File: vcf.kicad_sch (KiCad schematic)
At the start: 48 parts, among them Q4 BC307, U19 Opamp_Dual, U24 LM13700, U25 LM13700

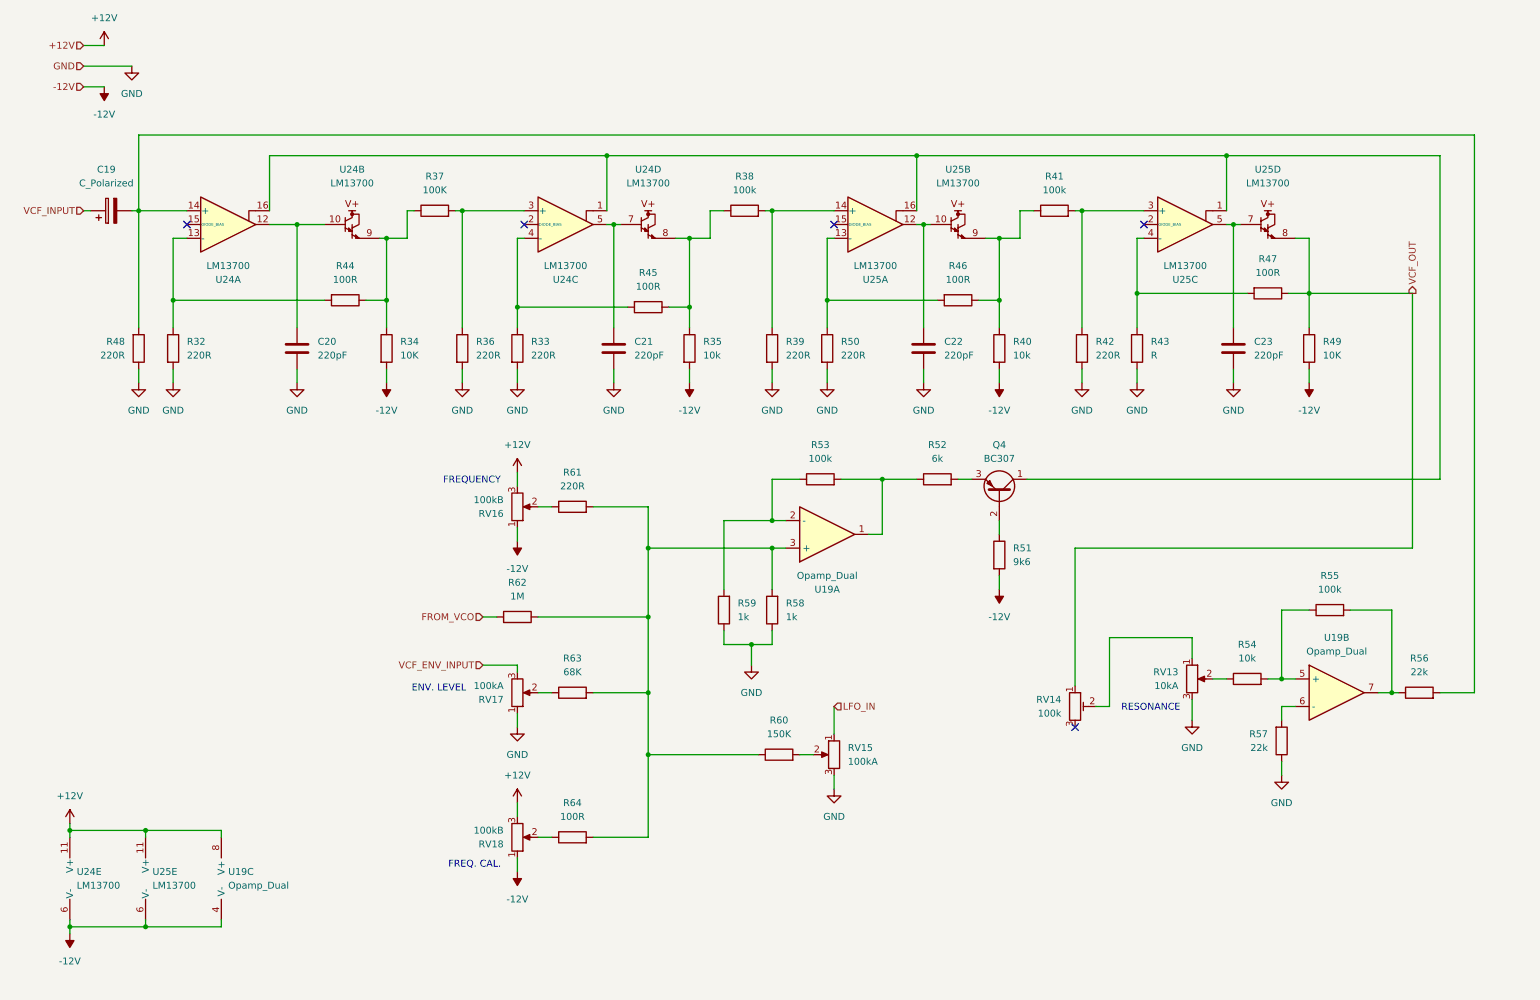
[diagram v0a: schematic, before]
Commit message: Add missing values and connectors
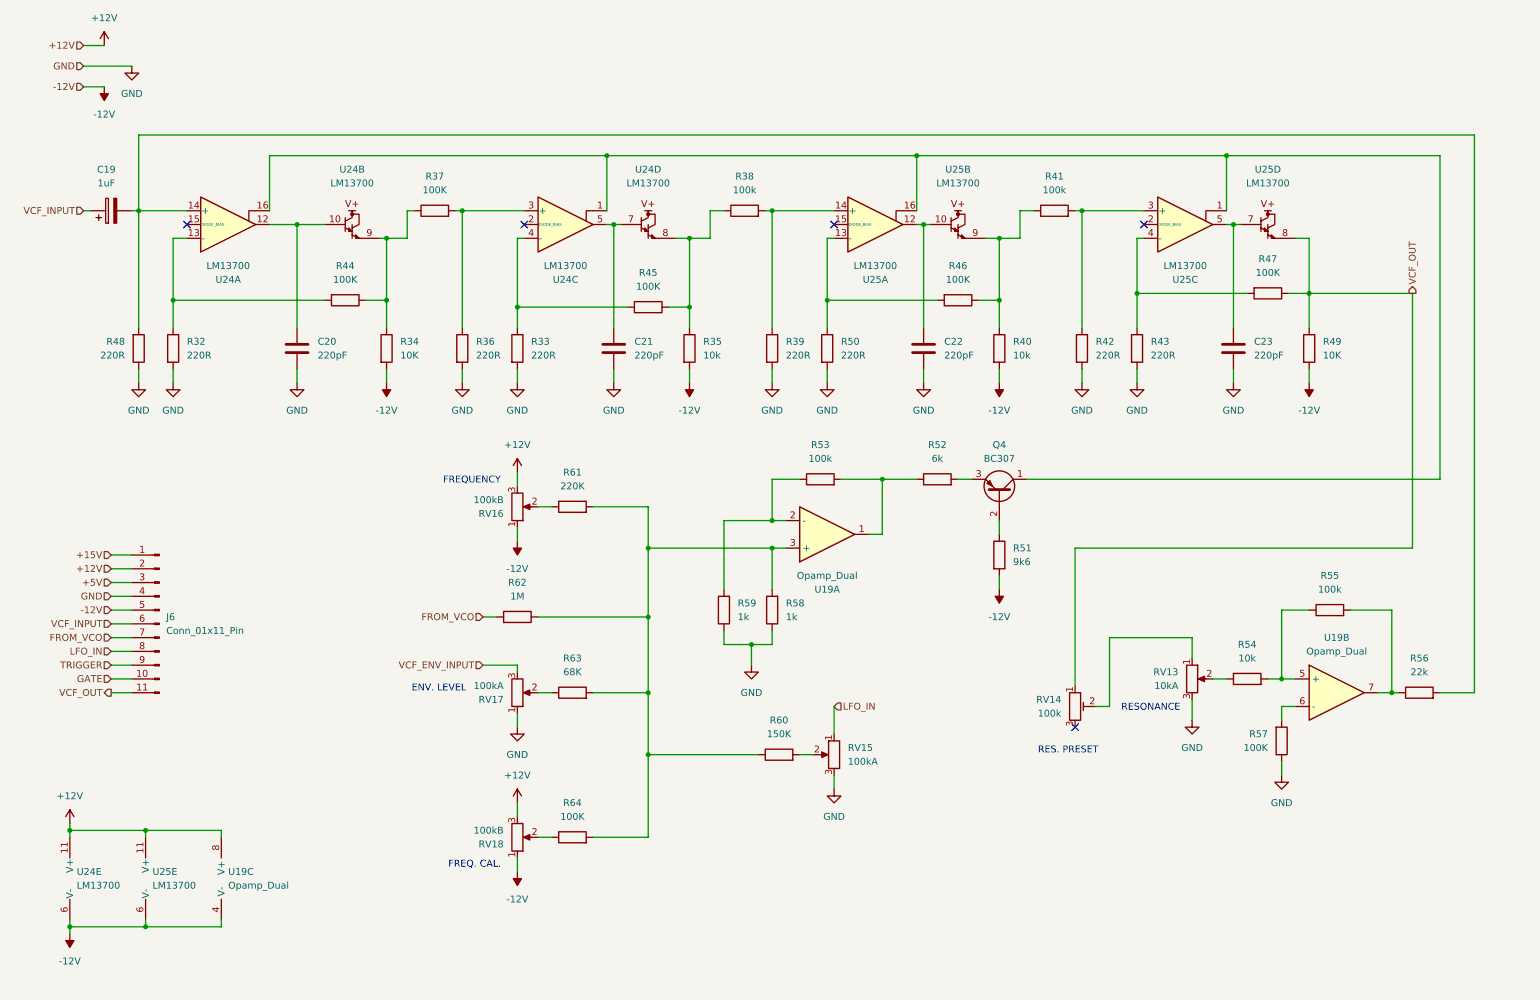
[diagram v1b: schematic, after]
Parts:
- added J6: Conn_01x11_Pin, symbol Connector:Conn_01x11_Pin
- C19: value C_Polarized -> 1uF
- R43: value R -> 220R
- R44, R45, R46, R47, R64: value 100R -> 100K
- R57: value 22k -> 100K
- R61: value 220R -> 220K
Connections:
- net +12V: now also J6.2 (Pin_2)
- net -12V: now also J6.5 (Pin_5)
- net FROM_VCO: now also J6.7 (Pin_7)
- net GND: now also J6.4 (Pin_4)
- net LFO_IN: now also J6.8 (Pin_8)
- net VCF_INPUT: now also J6.6 (Pin_6)
- net VCF_OUT: now also J6.11 (Pin_11)
- new net +15V: J6.1 (Pin_1)
- new net +5V: J6.3 (Pin_3)
- new net GATE: J6.10 (Pin_10)
- new net TRIGGER: J6.9 (Pin_9)
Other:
- note added: "RES. PRESET"

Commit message: Assign footprints and start PCB
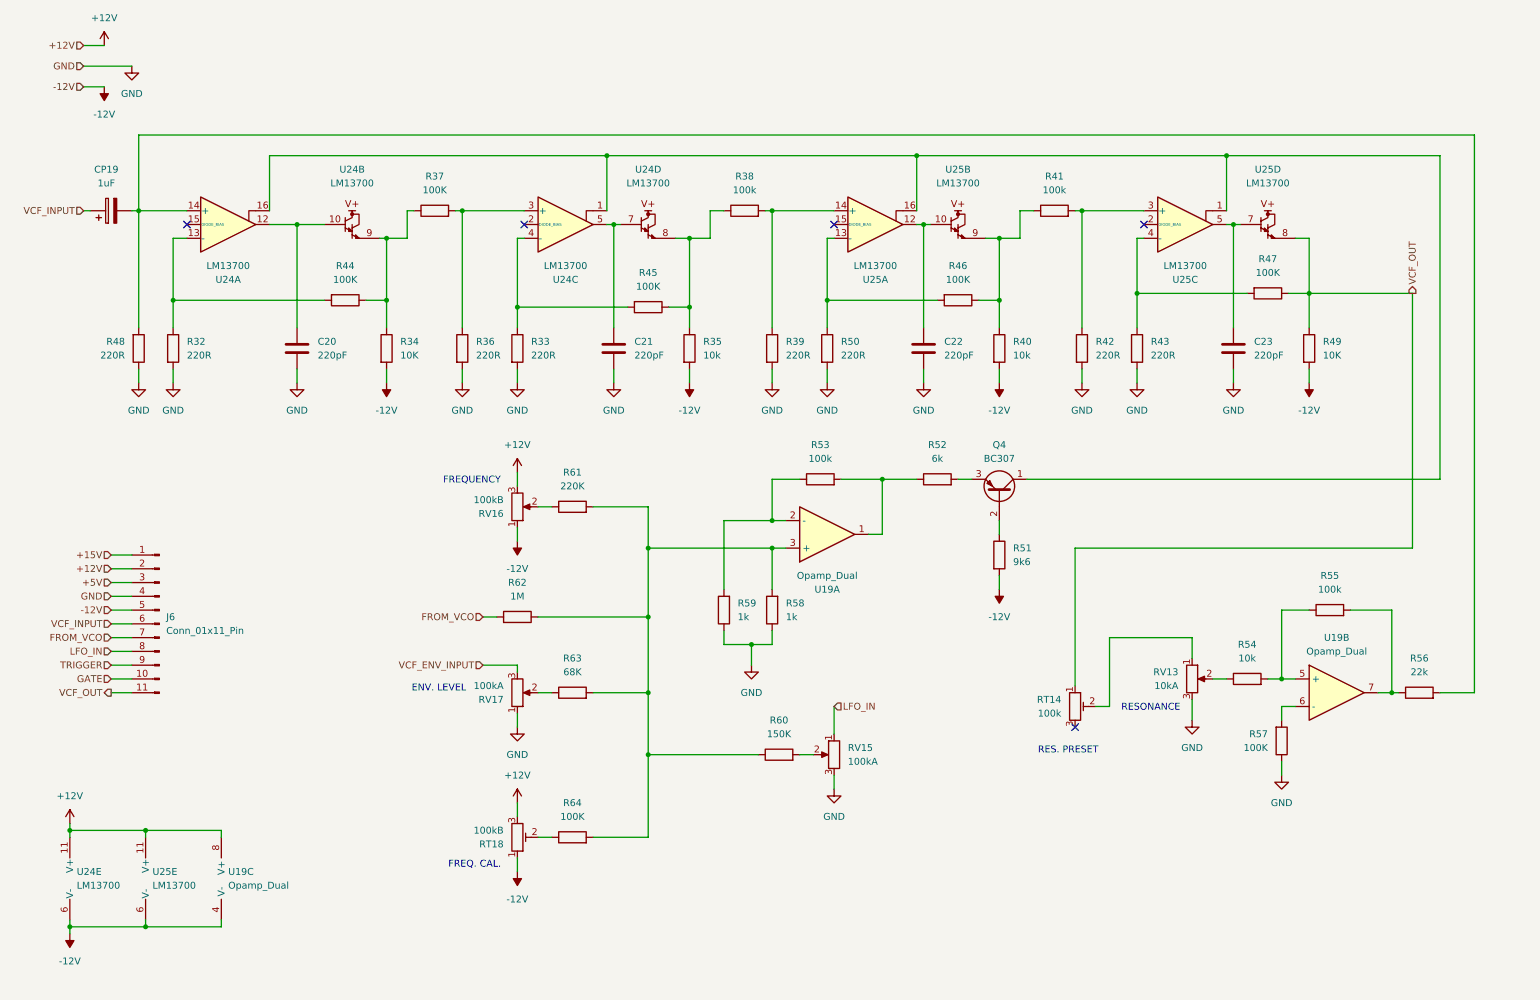
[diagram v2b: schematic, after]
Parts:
- C20, C21, C22, C23: footprint (none) -> Capacitor_THT:C_Disc_D5.0mm_W2.5mm_P5.00mm
- CP19: renamed from C19; footprint (none) -> Capacitor_THT:CP_Radial_D8.0mm_P3.80mm
- J6: footprint (none) -> Connector_PinHeader_2.54mm:PinHeader_1x11_P2.54mm_Vertical
- R32, R33, R34, R35, R36, R37, R38, R39, R40, R41, R42, R43, R44, R45, R46, R47, R48, R49, R50, R51, R52, R53, R54, R55, R56, R57, R58, R59, R60, R61, R62, R63, R64: footprint (none) -> Resistor_THT:R_Axial_DIN0204_L3.6mm_D1.6mm_P7.62mm_Horizontal
- RT14: renamed from RV14; footprint (none) -> Potentiometer_THT:Potentiometer_Bourns_3339P_Vertical_HandSoldering
- RT18: renamed from RV18; footprint (none) -> Potentiometer_THT:Potentiometer_Bourns_3339P_Vertical_HandSoldering; symbol Device:R_Potentiometer -> Device:R_Potentiometer_Trim
- RV13, RV15, RV16, RV17: footprint (none) -> Potentiometer_THT:Potentiometer_Omeg_PC16BU_Vertical
- U19: footprint (none) -> Package_DIP:DIP-8_W7.62mm_LongPads
- U24, U25: footprint (none) -> Package_DIP:DIP-16_W10.16mm_LongPads
